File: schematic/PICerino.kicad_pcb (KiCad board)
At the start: 2 copper layers, 95.2 x 111.8 mm, 16 parts, among them J1 Conn_01x05, J2 Conn_01x03, J3 PJ-079BH, J4 Conn_01x03, J5 USB_B, J6 10046971-001LF, J7 Conn_01x32, U1 PIC18LF45K50-I_P

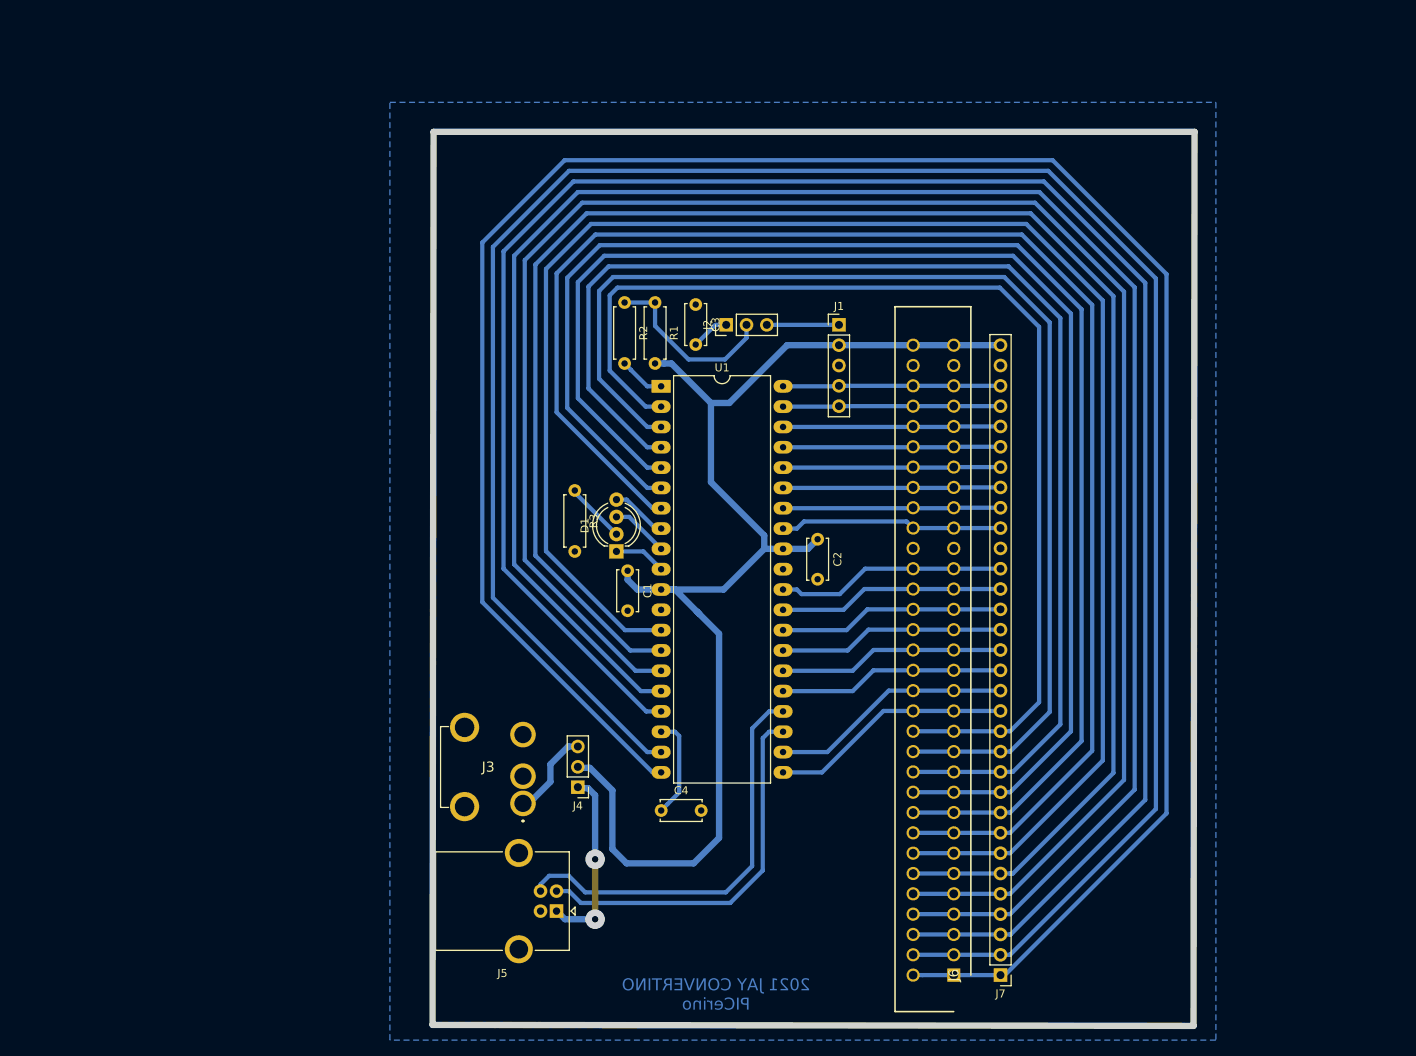
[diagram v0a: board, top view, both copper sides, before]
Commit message: expanded picerino to have 3 slots instead of 1. allowing multiple devices to be used.
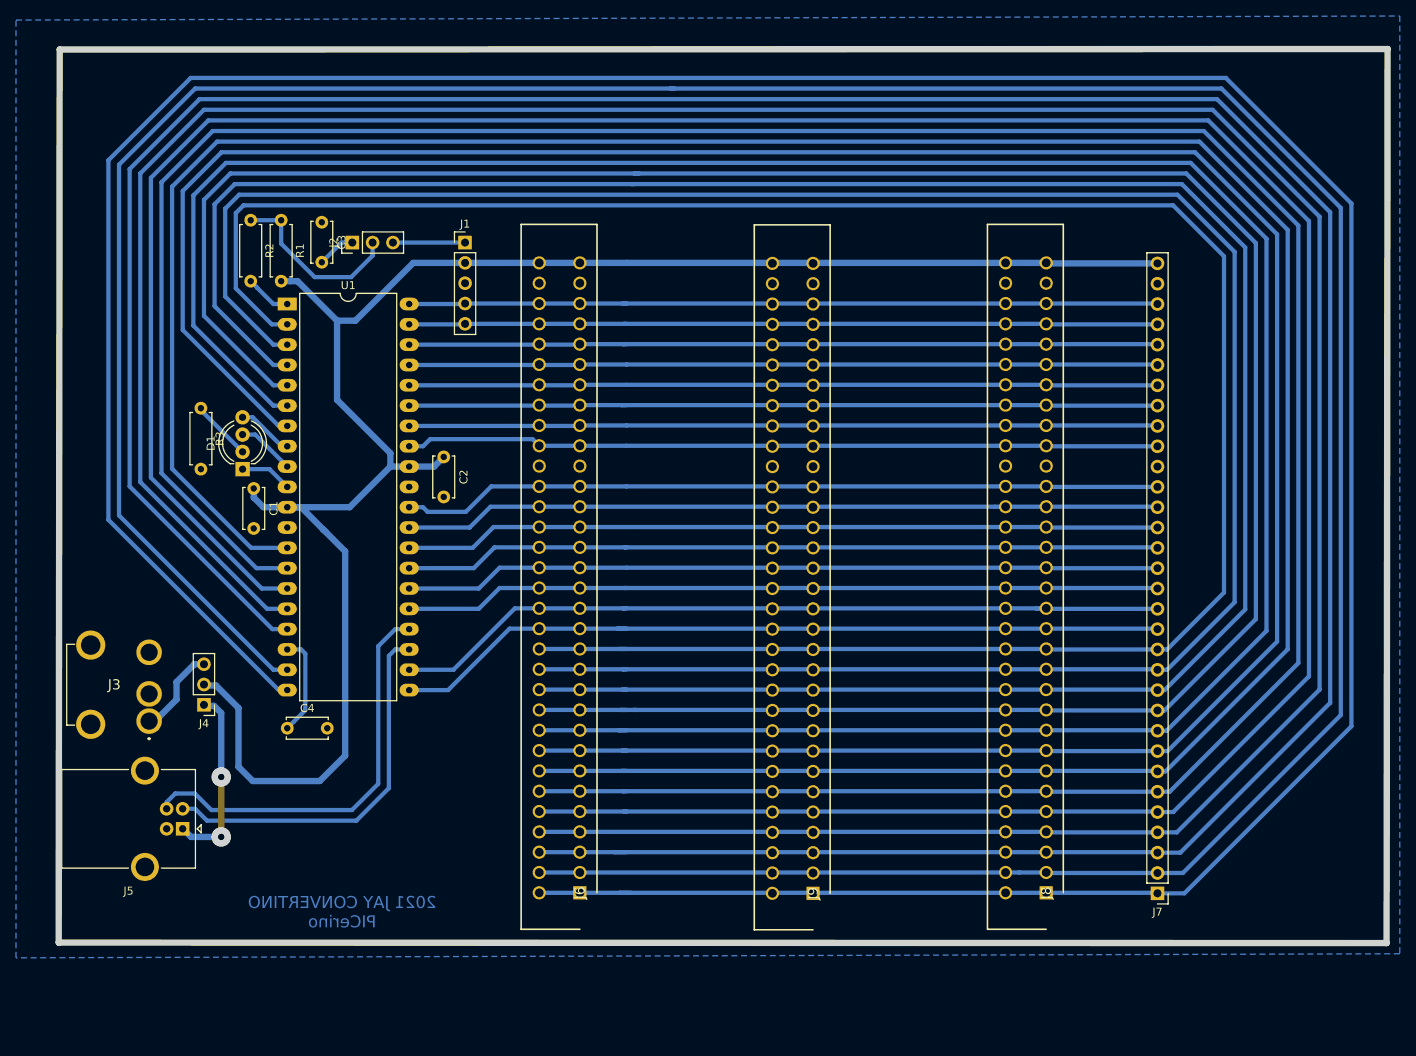
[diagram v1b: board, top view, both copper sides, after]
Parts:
- added J8: 10046971-001LF, 10046971-001LF:RHDR64W90P508X254_2X32_8786X929X1549P, F.Cu at (181.6, 136.0)
- added J9: 10046971-001LF, 10046971-001LF:RHDR64W90P508X254_2X32_8786X929X1549P, F.Cu at (152.5, 136.1)
- moved U1 47.9 mm to (86.7, 62.4)
- moved C1 47.9 mm to (82.5, 85.5)
- moved C4 47.9 mm to (86.7, 115.4)
- moved J1 47.9 mm to (109.0, 54.7)
- moved J3 47.9 mm to (69.5, 114.6)
- moved J4 47.9 mm to (76.3, 112.5)
- moved J5 47.9 mm to (73.7, 128.0)
- moved J6 47.9 mm to (123.3, 136.0)
- moved R1 47.9 mm to (86.0, 51.9)
- moved R2 47.9 mm to (82.2, 51.9)
- moved R3 47.9 mm to (75.9, 75.4)
- moved C2 47.9 mm to (106.3, 81.5)
- moved C3 47.9 mm to (91.1, 52.2)
- moved D1 47.9 mm to (81.2, 83.1)
- moved J2 47.9 mm to (94.9, 54.7)
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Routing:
- net /RD1: track 279.3 -> 419.2 mm
- net /RC2: track 256.5 -> 395.8 mm
- net /RD0: track 269.5 -> 408.0 mm
- net /RA6: track 226.1 -> 364.1 mm
- net /RA0: track 138.0 -> 275.8 mm
- net /RA4: track 180.2 -> 318.0 mm
- net /RC0: track 236.0 -> 373.7 mm
- net /RA3: track 170.4 -> 308.0 mm
- net /RC1: track 246.2 -> 383.8 mm
- net /RA5: track 190.4 -> 327.8 mm
- net /RA2: track 159.2 -> 296.6 mm
- net /RA7: track 215.7 -> 353.0 mm
- net /RA1: track 148.4 -> 285.8 mm
- net Net-(J6-Pad15): track 30.4 -> 98.4 mm
- net Net-(J6-Pad14): track 30.4 -> 97.9 mm
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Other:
- board size 95.2 x 111.8 mm -> 166.1 x 111.8 mm
